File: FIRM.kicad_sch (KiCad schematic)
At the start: 98 parts, among them J1 Conn_01x02_Pin, J2 DM3CS-SF, Q2 IRLML6402, SW1 PTS815, U1 STM32F405RGTx, U2 MIC5219-3.3YM5, U6 A-USBC-20F0-EA-GSR05, U7 W25Q128JVS, X2 32.768khz, Y1 12 MHz

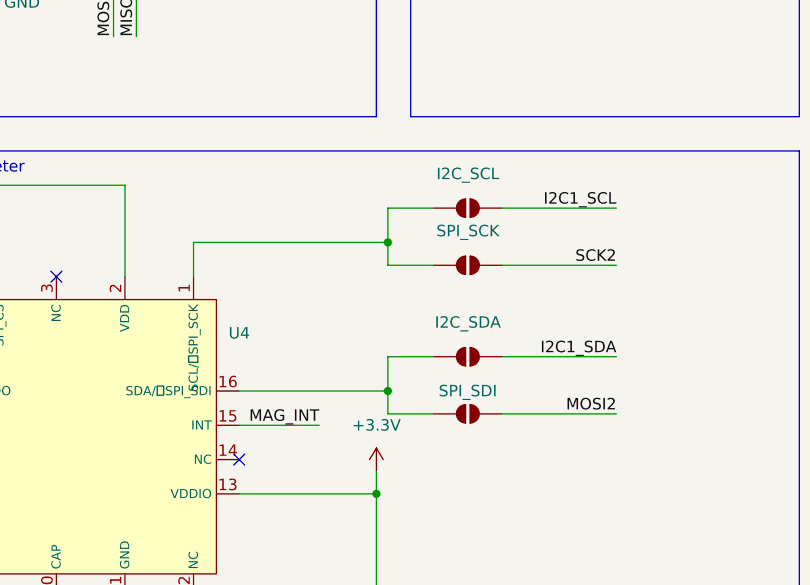
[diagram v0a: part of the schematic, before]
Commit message: Removed Jumpers from SCL & SDA of Magnetometer
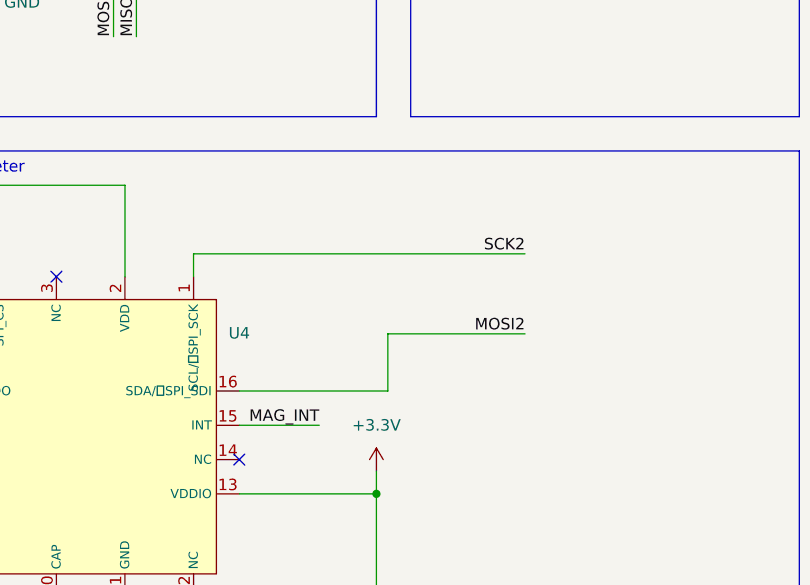
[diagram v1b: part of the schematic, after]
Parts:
- removed JP1: I2C_SDA, Jumper:SolderJumper-2_P1.3mm_Open_RoundedPad1.0x1.5mm, symbol Jumper:SolderJumper_2_Open
- removed JP2: SPI_SDI, Jumper:SolderJumper-2_P1.3mm_Open_RoundedPad1.0x1.5mm, symbol Jumper:SolderJumper_2_Open
- removed JP3: I2C_SCL, Jumper:SolderJumper-2_P1.3mm_Open_RoundedPad1.0x1.5mm, symbol Jumper:SolderJumper_2_Open
- removed JP4: SPI_SCK, Jumper:SolderJumper-2_P1.3mm_Open_RoundedPad1.0x1.5mm, symbol Jumper:SolderJumper_2_Open
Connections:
- net MOSI2: now also U4.16 (SDA/ SPI_SDI)
- net SCK2: now also U4.1 (SCL/ SPI_SCK)
